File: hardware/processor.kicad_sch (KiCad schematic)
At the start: 8 parts, among them J6 DEBUG, U1 STM32F411RETx

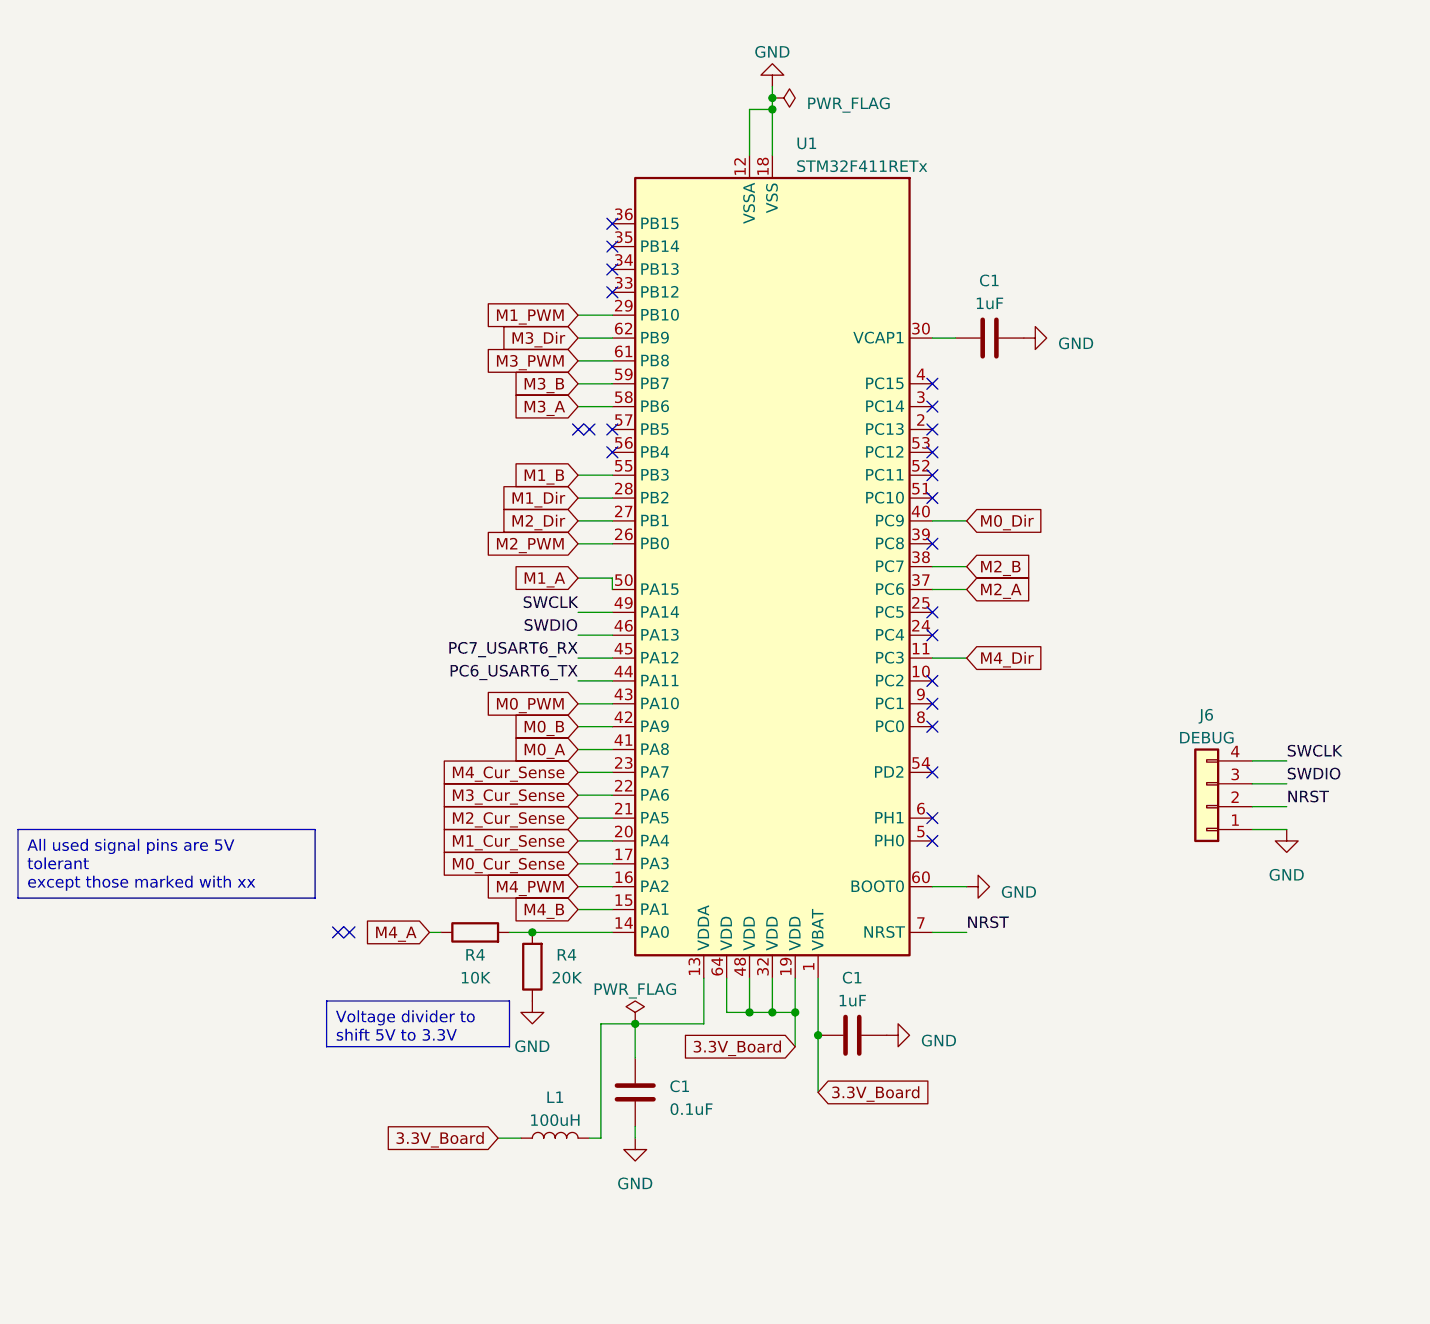
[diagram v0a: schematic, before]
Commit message: Change STM code to support an I2C bus. Add encoder reading code - tested on TIM1.
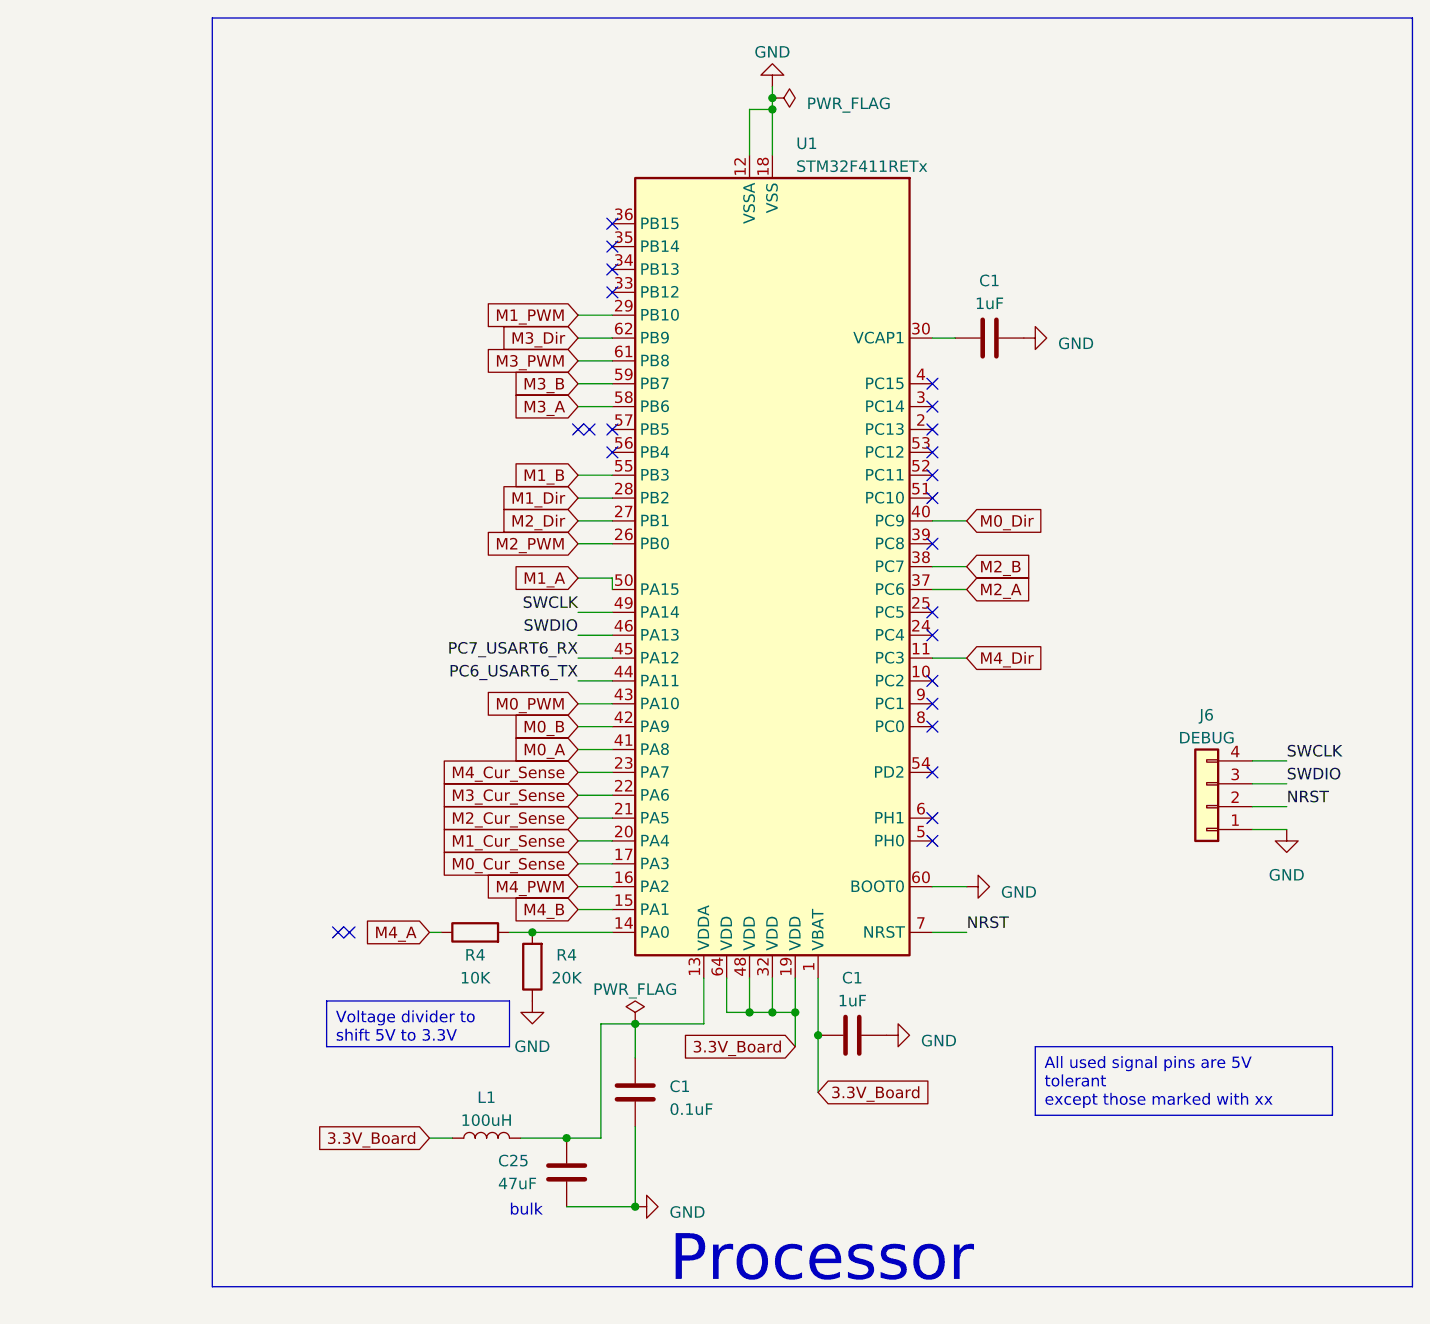
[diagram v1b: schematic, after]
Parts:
- added C25: 47uF, Capacitor_SMD:C_0805_2012Metric, symbol Device:C
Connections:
- net GND: now also C25.2
- net at C1.2, L1.2, U1.13 (VDDA): now also C25.1
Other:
- note added: "Processor"
- note added: "bulk"
- moved on the sheet: L1
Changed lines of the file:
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@@
   (junction (at 121.92 135.89) (diameter 0) (color 0 0 0 0)
   )
+  (junction (at 93.98 147.32) (diameter 0) (color 0 0 0 0)
+  )
   (junction (at 119.38 133.35) (diameter 0) (color 0 0 0 0)
   )
@@
   )
   (junction (at 101.6 134.62) (diameter 0) (color 0 0 0 0)
+  )
+  (junction (at 101.6 154.94) (diameter 0) (color 0 0 0 0)
   )
   (junction (at 116.84 33.02) (diameter 0) (color 0 0 0 0)
@@
     (stroke (width 0) (type default))
   )
-  (wire (pts (xy 101.6 147.32) (xy 101.6 146.05))
+  (wire (pts (xy 101.6 154.94) (xy 101.6 146.05))
     (stroke (width 0) (type default))
   )
@@
     (stroke (width 0) (type default))
   )
-  (wire (pts (xy 97.79 147.32) (xy 96.52 147.32))
+  (wire (pts (xy 97.79 147.32) (xy 93.98 147.32))
     (stroke (width 0) (type default))
   )
@@
     (stroke (width 0) (type default))
   )
-  (wire (pts (xy 86.36 147.32) (xy 88.9 147.32))
+  (wire (pts (xy 78.74 147.32) (xy 81.28 147.32))
     (stroke (width 0) (type default))
   )
@@
     (stroke (width 0) (type default))
   )
+  (wire (pts (xy 93.98 154.94) (xy 101.6 154.94))
+    (stroke (width 0) (type default))
+  )
   (wire (pts (xy 116.84 31.75) (xy 116.84 33.02))
     (stroke (width 0) (type default))
@@
     (stroke (width 0) (type default))
   )
+  (wire (pts (xy 88.9 147.32) (xy 93.98 147.32))
+    (stroke (width 0) (type default))
+  )
   (wire (pts (xy 95.25 60.96) (xy 99.06 60.96))
     (stroke (width 0) (type default))
@@
   (wire (pts (xy 90.17 124.46) (xy 99.06 124.46))
     (stroke (width 0) (type default))
+  )
+  (rectangle (start 54.61 22.86) (end 187.96 163.83)
+    (stroke (width 0) (type default))
+    (fill (type none))
   )
   (text_box "Voltage divider to shift 5V to 3.3V"
@@
   )
   (text_box "All used signal pins are 5V tolerant\nexcept those marked with xx"
-    (at 33.02 113.03 0) (size 33.02 7.62)
+    (at 146.05 137.16 0) (size 33.02 7.62)
     (stroke (width 0) (type default))
     (fill (type none))
     (effects (font (size 1.27 1.27)) (justify left top))
+  )
+  (text "Processor" (at 105.41 163.83 0)
+    (effects (font (size 5.08 5.08)) (justify left bottom))
+  )
+  (text "bulk" (at 87.63 156.21 0)
+    (effects (font (size 1.27 1.27)) (justify left bottom))
   )
   (label "PC6_USART6_TX" (at 95.25 96.52 180) (fields_autoplaced)
@@
     )
   )
-  (global_label "3.3V_Board" (shape input) (at 86.36 147.32 180) (fields_autoplaced)
-    (effects (font (size 1.27 1.27)) (justify right))
-    (property "Intersheetrefs" "${INTERSHEET_REFS}" (at 72.871 147.32 0)
+  (global_label "3.3V_Board" (shape input) (at 78.74 147.32 180) (fields_autoplaced)
+    (effects (font (size 1.27 1.27)) (justify right))
+    (property "Intersheetrefs" "${INTERSHEET_REFS}" (at 65.251 147.32 0)
       (effects (font (size 1.27 1.27)) (justify right) hide)
     )
@@
     )
   )
-  (symbol (lib_id "power:GND") (at 101.6 147.32 0) (unit 1)
+  (symbol (lib_id "power:GND") (at 101.6 154.94 90) (unit 1)
     (in_bom yes) (on_board yes) (dnp no) (fields_autoplaced)
-    (property "Reference" "#PWR06" (at 101.6 153.67 0)
-      (effects (font (size 1.27 1.27)) hide)
-    )
-    (property "Value" "GND" (at 101.6 152.4 0)
-      (effects (font (size 1.27 1.27)))
-    )
-    (property "Footprint" "" (at 101.6 147.32 0)
-      (effects (font (size 1.27 1.27)) hide)
-    )
-    (property "Datasheet" "" (at 101.6 147.32 0)
+    (property "Reference" "#PWR06" (at 107.95 154.94 0)
+      (effects (font (size 1.27 1.27)) hide)
+    )
+    (property "Value" "GND" (at 105.41 155.575 90)
+      (effects (font (size 1.27 1.27)) (justify right))
+    )
+    (property "Footprint" "" (at 101.6 154.94 0)
+      (effects (font (size 1.27 1.27)) hide)
+    )
+    (property "Datasheet" "" (at 101.6 154.94 0)
       (effects (font (size 1.27 1.27)) hide)
     )
@@
     )
   )
-  (symbol (lib_id "Device:L") (at 92.71 147.32 90) (unit 1)
+  (symbol (lib_id "Device:L") (at 85.09 147.32 90) (unit 1)
     (in_bom yes) (on_board yes) (dnp no) (fields_autoplaced)
-    (property "Reference" "L1" (at 92.71 142.8242 90)
+    (property "Reference" "L1" (at 85.09 142.8242 90)
       (effects (font (size 1.27 1.27)))
     )
-    (property "Value" "100uH" (at 92.71 145.3642 90)
+    (property "Value" "100uH" (at 85.09 145.3642 90)
       (effects (font (size 1.27 1.27)))
     )
-    (property "Footprint" "Inductor_SMD:L_0805_2012Metric" (at 92.71 147.32 0)
-      (effects (font (size 1.27 1.27)) hide)
-    )
-    (property "Datasheet" "~" (at 92.71 147.32 0)
+    (property "Footprint" "Inductor_SMD:L_0805_2012Metric" (at 85.09 147.32 0)
+      (effects (font (size 1.27 1.27)) hide)
+    )
+    (property "Datasheet" "~" (at 85.09 147.32 0)
       (effects (font (size 1.27 1.27)) hide)
     )
@@
         )
       )
+    )
+  )
+  (symbol (lib_id "Device:C") (at 93.98 151.13 0) (unit 1)
+    (in_bom yes) (on_board yes) (dnp no)
+    (property "Reference" "C25" (at 86.36 149.86 0)
+      (effects (font (size 1.27 1.27)) (justify left))
+    )
+    (property "Value" "47uF" (at 86.36 152.4 0)
+      (effects (font (size 1.27 1.27)) (justify left))
+    )
+    (property "Footprint" "Capacitor_SMD:C_0805_2012Metric" (at 94.9452 154.94 0)
+      (effects (font (size 1.27 1.27)) hide)
+    )
+    (property "Datasheet" "~" (at 93.98 151.13 0)
+      (effects (font (size 1.27 1.27)) hide)
+    )
+    (pin "1")
+    (pin "2")
+    (instances
+      (project "rangefinder2"
+        (path "/0b3e5813-673f-4f67-83c8-f01b9503b5c1/2017639a-2389-4cf2-aeb2-8a719e2bc2bc"
+          (reference "C25") (unit 1)
+        )
+      )
+      (project "Rangefinder"
+        (path "/1a7ff774-b73f-44dc-80af-cc4169dc627d/6680126b-7f85-43b7-9d8b-096577af4c5b"
+          (reference "C14") (unit 1)
+        )
+      )
+      (project "HapticHandsV2"
+        (path "/39a4a7a0-ffc4-4861-b33d-34da3c27e7e8/f3252ed2-35ae-42bb-a4d7-15f17536fa50"
+          (reference "C27") (unit 1)
+        )
+        (path "/39a4a7a0-ffc4-4861-b33d-34da3c27e7e8/3b9177ca-97cd-47b7-a3ec-5363b3c1395f"
+          (reference "C28") (unit 1)
+        )
+      )

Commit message: Add past project scripts. Add more lib components.
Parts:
- added J11: I2C_SCL_Testpoint, SamacSys_Parts:5000, symbol SamacSys_Parts:5000
- added J12: I2C_SDA_Testpoint, SamacSys_Parts:5000, symbol SamacSys_Parts:5000
- added J18: SPARE, symbol Connector_Generic:Conn_01x05
- added R4 (x2): 2.2K, Resistor_SMD:R_0402_1005Metric, symbol Device:R
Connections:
- net 3.3V_Board: now also R4.2, R4.2
- net GPIO2: now reaches U1.2 (PC13)
- net GPIO2: now also J18.3 (Pin_3)
- net GPIO1: now reaches U1.3 (PC14)
- net GPIO1: now also J18.4 (Pin_4)
- net GPIO0: now reaches U1.4 (PC15)
- net GPIO0: now also J18.5 (Pin_5)
- net GPIO4: now reaches U1.52 (PC11)
- net GPIO4: now also J18.1 (Pin_1)
- net GPIO3: now reaches U1.53 (PC12)
- net GPIO3: now also J18.2 (Pin_2)
- net M0_Dir: no longer names the net of U1.40 (PC9)
- net M0_PWM: no longer names the net of U1.43 (PA10)
- net M1_Dir: no longer names the net of U1.28 (PB2)
- net M1_PWM: no longer names the net of U1.29 (PB10)
- net M2_Dir: no longer names the net of U1.27 (PB1)
- net M2_PWM: no longer names the net of U1.26 (PB0)
- net M3_Dir renamed I2C_SDA
- net I2C_SDA: now also J12.1, R4.1
- net M3_PWM renamed I2C_SCL
- net I2C_SCL: now also J11.1, R4.1
- net M4_Dir: no longer names the net of U1.11 (PC3)
- net M4_PWM: no longer names the net of U1.16 (PA2)
- no-connect marks 25 -> 29
